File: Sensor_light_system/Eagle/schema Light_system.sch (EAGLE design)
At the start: 11 parts, among them IC1 STM32F030C8T6TR, J1 12_WAY_CON

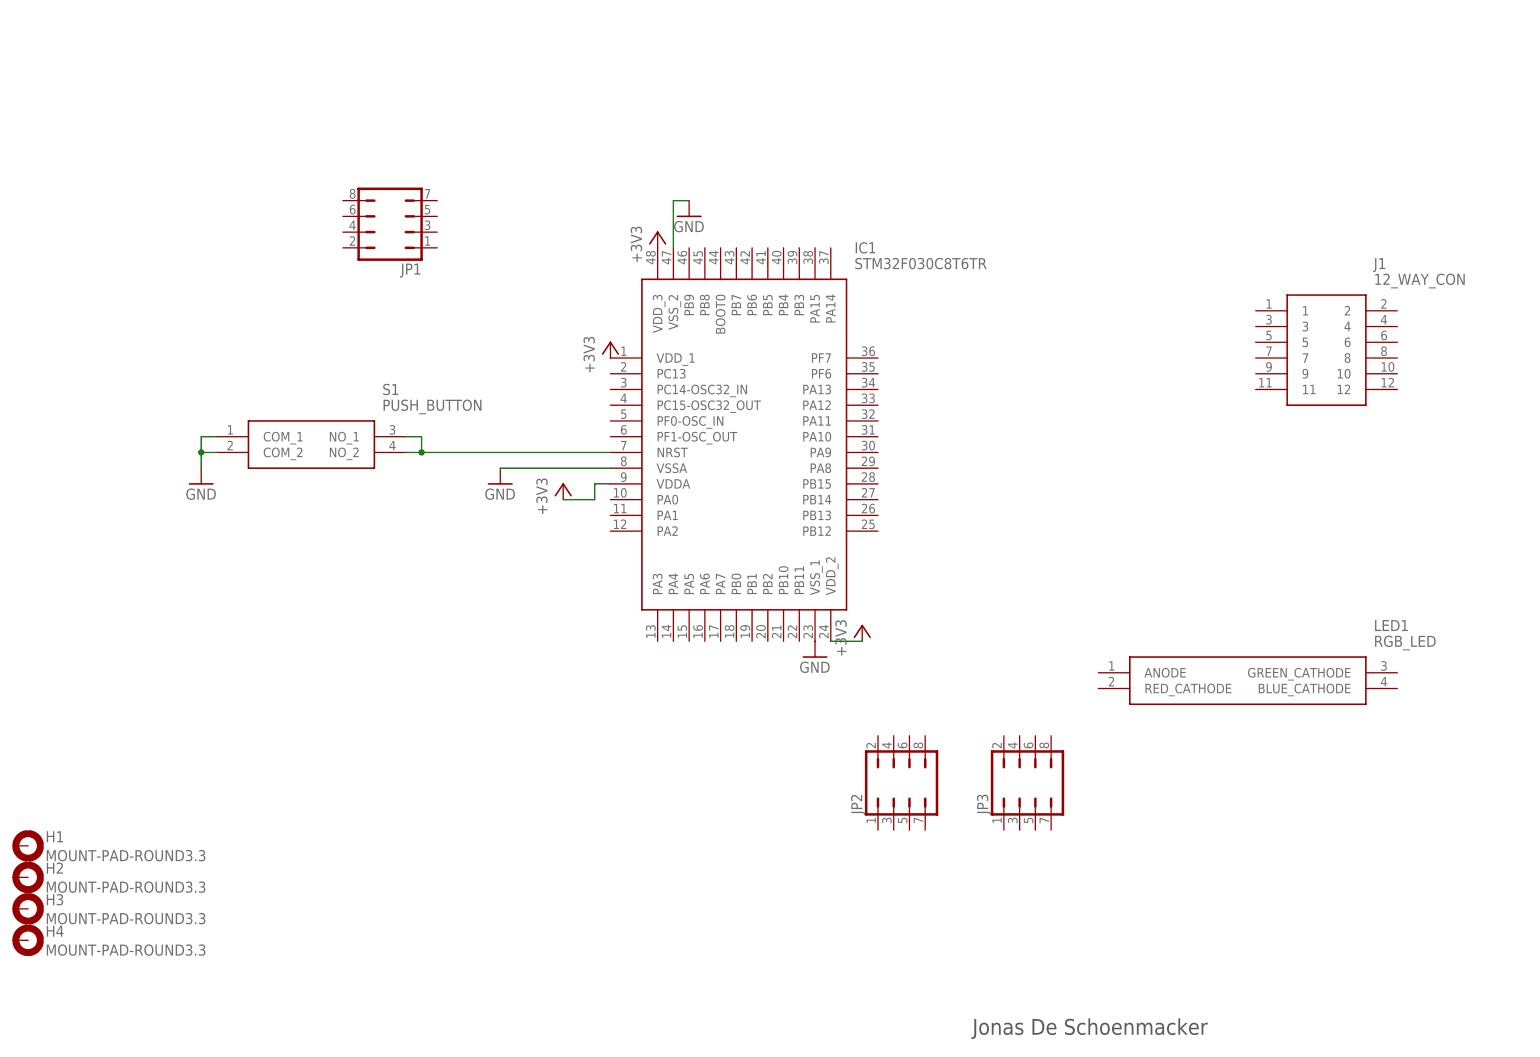
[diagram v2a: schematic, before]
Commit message: schema sensor
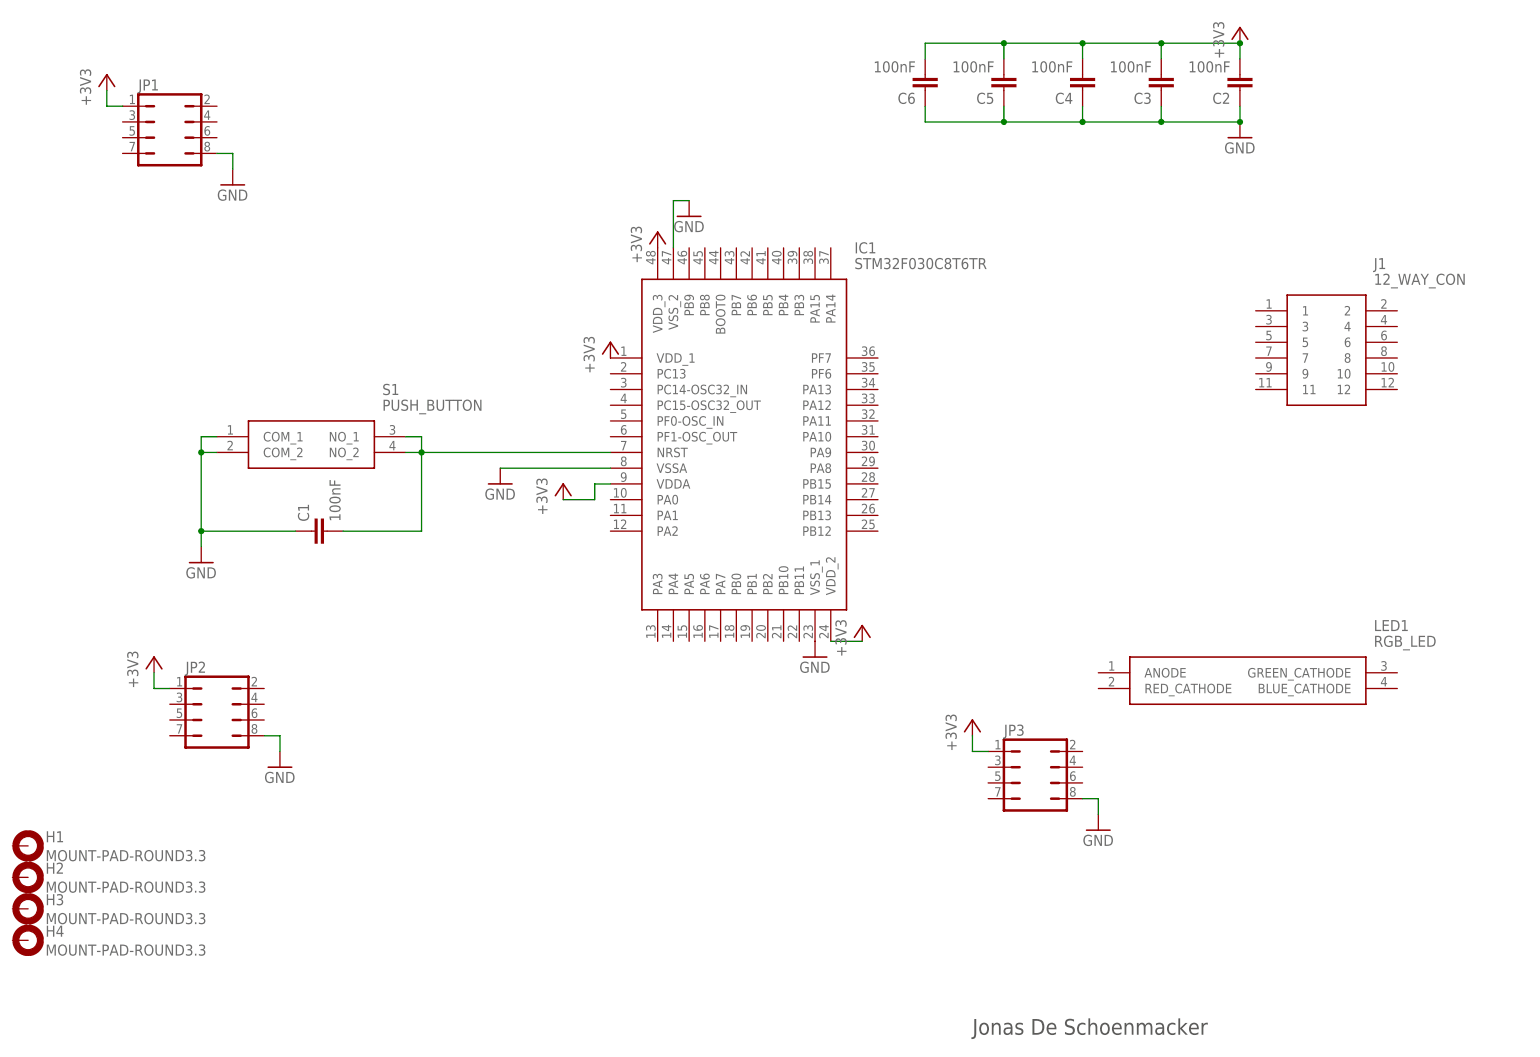
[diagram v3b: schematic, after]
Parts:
- added C1, C2, C3, C4, C5, C6: 100nF, resistor:C-EUC1206
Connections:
- new net OSC_IN: C2.2
- new net OSC_OUT: C1.2
- net +3V3: now also C2.2, C3.2, C4.1, C4.2, C5.1, C5.2, C6.1, C6.2
- net GND: now also C1.1, C2.1, C3.1, C3.2, C4.1, C4.2, C5.1, C5.2, C6.1, C6.2, JP1.8, JP2.8, JP3.8
- net N$3: now also C1.2
- net N$6: now also C3.1
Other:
- moved on the sheet: JP1, JP2, JP3
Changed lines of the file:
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@@
 <part name="JP2" library="jumper" deviceset="JP4Q" device=""/>
 <part name="JP3" library="jumper" deviceset="JP4Q" device=""/>
+<part name="+3V5" library="supply1" deviceset="+3V3" device=""/>
+<part name="GND5" library="supply1" deviceset="GND" device=""/>
+<part name="C1" library="resistor" deviceset="C-EU" device="C1206" value="100nF"/>
+<part name="+3V6" library="supply1" deviceset="+3V3" device=""/>
+<part name="C2" library="resistor" deviceset="C-EU" device="C1206" value="100nF"/>
+<part name="C3" library="resistor" deviceset="C-EU" device="C1206" value="100nF"/>
+<part name="C4" library="resistor" deviceset="C-EU" device="C1206" value="100nF"/>
+<part name="C5" library="resistor" deviceset="C-EU" device="C1206" value="100nF"/>
+<part name="C6" library="resistor" deviceset="C-EU" device="C1206" value="100nF"/>
+<part name="GND6" library="supply1" deviceset="GND" device=""/>
+<part name="+3V7" library="supply1" deviceset="+3V3" device=""/>
+<part name="GND7" library="supply1" deviceset="GND" device=""/>
+<part name="GND8" library="supply1" deviceset="GND" device=""/>
+<part name="+3V8" library="supply1" deviceset="+3V3" device=""/>
 </parts>
 <sheets>
@@
 <attribute name="VALUE" x="96.52" y="91.44" size="1.778" layer="96" rot="R90"/>
 </instance>
-<instance part="GND4" gate="1" x="40.64" y="96.52">
-<attribute name="VALUE" x="38.1" y="93.98" size="1.778" layer="96"/>
-</instance>
-<instance part="JP1" gate="B" x="71.12" y="137.16" rot="R90"/>
-<instance part="JP2" gate="B" x="152.4" y="48.26"/>
-<instance part="JP3" gate="B" x="172.72" y="48.26"/>
+<instance part="GND4" gate="1" x="40.64" y="83.82">
+<attribute name="VALUE" x="38.1" y="81.28" size="1.778" layer="96"/>
+</instance>
+<instance part="JP1" gate="B" x="35.56" y="154.94" rot="R270"/>
+<instance part="JP2" gate="B" x="43.18" y="60.96" rot="R270"/>
+<instance part="JP3" gate="B" x="175.26" y="50.8" rot="R270"/>
+<instance part="+3V5" gate="G$1" x="25.4" y="162.56">
+<attribute name="VALUE" x="22.86" y="157.48" size="1.778" layer="96" rot="R90"/>
+</instance>
+<instance part="GND5" gate="1" x="45.72" y="144.78">
+<attribute name="VALUE" x="43.18" y="142.24" size="1.778" layer="96"/>
+</instance>
+<instance part="C1" gate="G$1" x="58.42" y="88.9" rot="R90"/>
+<instance part="+3V6" gate="G$1" x="208.28" y="170.18">
+<attribute name="VALUE" x="205.74" y="165.1" size="1.778" layer="96" rot="R90"/>
+</instance>
+<instance part="C2" gate="G$1" x="208.28" y="160.02" rot="R180"/>
+<instance part="C3" gate="G$1" x="195.58" y="160.02" rot="R180"/>
+<instance part="C4" gate="G$1" x="182.88" y="160.02" rot="R180"/>
+<instance part="C5" gate="G$1" x="170.18" y="160.02" rot="R180"/>
+<instance part="C6" gate="G$1" x="157.48" y="160.02" rot="R180"/>
+<instance part="GND6" gate="1" x="208.28" y="152.4"/>
+<instance part="+3V7" gate="G$1" x="33.02" y="68.58">
+<attribute name="VALUE" x="30.48" y="63.5" size="1.778" layer="96" rot="R90"/>
+</instance>
+<instance part="GND7" gate="1" x="53.34" y="50.8">
+<attribute name="VALUE" x="50.8" y="48.26" size="1.778" layer="96"/>
+</instance>
+<instance part="GND8" gate="1" x="185.42" y="40.64">
+<attribute name="VALUE" x="182.88" y="38.1" size="1.778" layer="96"/>
+</instance>
+<instance part="+3V8" gate="G$1" x="165.1" y="58.42">
+<attribute name="VALUE" x="162.56" y="53.34" size="1.778" layer="96" rot="R90"/>
+</instance>
 </instances>
 <busses>
@@
 <pinref part="+3V2" gate="G$1" pin="+3V3"/>
 <wire x1="142.24" y1="71.12" x2="147.32" y2="71.12" width="0.1524" layer="91"/>
+</segment>
+<segment>
+<pinref part="+3V5" gate="G$1" pin="+3V3"/>
+<wire x1="25.4" y1="160.02" x2="25.4" y2="157.48" width="0.1524" layer="91"/>
+<pinref part="JP1" gate="B" pin="1"/>
+<wire x1="25.4" y1="157.48" x2="27.94" y2="157.48" width="0.1524" layer="91"/>
+</segment>
+<segment>
+<pinref part="+3V6" gate="G$1" pin="+3V3"/>
+<pinref part="C2" gate="G$1" pin="2"/>
+<wire x1="208.28" y1="167.64" x2="208.28" y2="165.1" width="0.1524" layer="91"/>
+<pinref part="C6" gate="G$1" pin="2"/>
+<wire x1="208.28" y1="167.64" x2="195.58" y2="167.64" width="0.1524" layer="91"/>
+<wire x1="195.58" y1="167.64" x2="182.88" y2="167.64" width="0.1524" layer="91"/>
+<wire x1="182.88" y1="167.64" x2="170.18" y2="167.64" width="0.1524" layer="91"/>
+<wire x1="170.18" y1="167.64" x2="157.48" y2="167.64" width="0.1524" layer="91"/>
+<wire x1="157.48" y1="167.64" x2="157.48" y2="165.1" width="0.1524" layer="91"/>
+<junction x="208.28" y="167.64"/>
+<pinref part="C5" gate="G$1" pin="2"/>
+<wire x1="170.18" y1="165.1" x2="170.18" y2="167.64" width="0.1524" layer="91"/>
+<junction x="170.18" y="167.64"/>
+<pinref part="C4" gate="G$1" pin="2"/>
+<wire x1="182.88" y1="165.1" x2="182.88" y2="167.64" width="0.1524" layer="91"/>
+<junction x="182.88" y="167.64"/>
+<pinref part="C3" gate="G$1" pin="2"/>
+<wire x1="195.58" y1="165.1" x2="195.58" y2="167.64" width="0.1524" layer="91"/>
+<junction x="195.58" y="167.64"/>
+</segment>
+<segment>
+<pinref part="+3V7" gate="G$1" pin="+3V3"/>
+<wire x1="33.02" y1="66.04" x2="33.02" y2="63.5" width="0.1524" layer="91"/>
+<pinref part="JP2" gate="B" pin="1"/>
+<wire x1="33.02" y1="63.5" x2="35.56" y2="63.5" width="0.1524" layer="91"/>
+</segment>
+<segment>
+<pinref part="JP3" gate="B" pin="1"/>
+<wire x1="167.64" y1="53.34" x2="165.1" y2="53.34" width="0.1524" layer="91"/>
+<pinref part="+3V8" gate="G$1" pin="+3V3"/>
+<wire x1="165.1" y1="53.34" x2="165.1" y2="55.88" width="0.1524" layer="91"/>
 </segment>
 </net>
@@
 <wire x1="40.64" y1="101.6" x2="43.18" y2="101.6" width="0.1524" layer="91"/>
 <pinref part="GND4" gate="1" pin="GND"/>
-<wire x1="40.64" y1="99.06" x2="40.64" y2="101.6" width="0.1524" layer="91"/>
+<wire x1="40.64" y1="86.36" x2="40.64" y2="88.9" width="0.1524" layer="91"/>
 <junction x="40.64" y="101.6"/>
+<pinref part="C1" gate="G$1" pin="1"/>
+<wire x1="40.64" y1="88.9" x2="40.64" y2="101.6" width="0.1524" layer="91"/>
+<wire x1="55.88" y1="88.9" x2="40.64" y2="88.9" width="0.1524" layer="91"/>
+<junction x="40.64" y="88.9"/>
+</segment>
+<segment>
+<pinref part="JP1" gate="B" pin="8"/>
+<wire x1="43.18" y1="149.86" x2="45.72" y2="149.86" width="0.1524" layer="91"/>
+<pinref part="GND5" gate="1" pin="GND"/>
+<wire x1="45.72" y1="149.86" x2="45.72" y2="147.32" width="0.1524" layer="91"/>
+</segment>
+<segment>
+<pinref part="C6" gate="G$1" pin="1"/>
+<wire x1="157.48" y1="157.48" x2="157.48" y2="154.94" width="0.1524" layer="91"/>
+<pinref part="C2" gate="G$1" pin="1"/>
+<wire x1="157.48" y1="154.94" x2="170.18" y2="154.94" width="0.1524" layer="91"/>
+<wire x1="170.18" y1="154.94" x2="182.88" y2="154.94" width="0.1524" layer="91"/>
+<wire x1="182.88" y1="154.94" x2="195.58" y2="154.94" width="0.1524" layer="91"/>
+<wire x1="195.58" y1="154.94" x2="208.28" y2="154.94" width="0.1524" layer="91"/>
+<wire x1="208.28" y1="154.94" x2="208.28" y2="157.48" width="0.1524" layer="91"/>
+<pinref part="C3" gate="G$1" pin="1"/>
+<wire x1="195.58" y1="157.48" x2="195.58" y2="154.94" width="0.1524" layer="91"/>
+<junction x="195.58" y="154.94"/>
+<pinref part="C4" gate="G$1" pin="1"/>
+<wire x1="182.88" y1="157.48" x2="182.88" y2="154.94" width="0.1524" layer="91"/>
+<junction x="182.88" y="154.94"/>
+<pinref part="C5" gate="G$1" pin="1"/>
+<wire x1="170.18" y1="157.48" x2="170.18" y2="154.94" width="0.1524" layer="91"/>
+<junction x="170.18" y="154.94"/>
+<pinref part="GND6" gate="1" pin="GND"/>
+<junction x="208.28" y="154.94"/>
+</segment>
+<segment>
+<pinref part="JP2" gate="B" pin="8"/>
+<wire x1="50.8" y1="55.88" x2="53.34" y2="55.88" width="0.1524" layer="91"/>
+<pinref part="GND7" gate="1" pin="GND"/>
+<wire x1="53.34" y1="55.88" x2="53.34" y2="53.34" width="0.1524" layer="91"/>
+</segment>
+<segment>
+<pinref part="JP3" gate="B" pin="8"/>
+<wire x1="182.88" y1="45.72" x2="185.42" y2="45.72" width="0.1524" layer="91"/>
+<pinref part="GND8" gate="1" pin="GND"/>
+<wire x1="185.42" y1="45.72" x2="185.42" y2="43.18" width="0.1524" layer="91"/>
 </segment>
 </net>
@@
 <wire x1="106.68" y1="101.6" x2="76.2" y2="101.6" width="0.1524" layer="91"/>
 <junction x="76.2" y="101.6"/>
+<pinref part="C1" gate="G$1" pin="2"/>
+<wire x1="63.5" y1="88.9" x2="76.2" y2="88.9" width="0.1524" layer="91"/>
+<wire x1="76.2" y1="88.9" x2="76.2" y2="101.6" width="0.1524" layer="91"/>
 </segment>
 </net>

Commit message: schema sensor gewijzigd
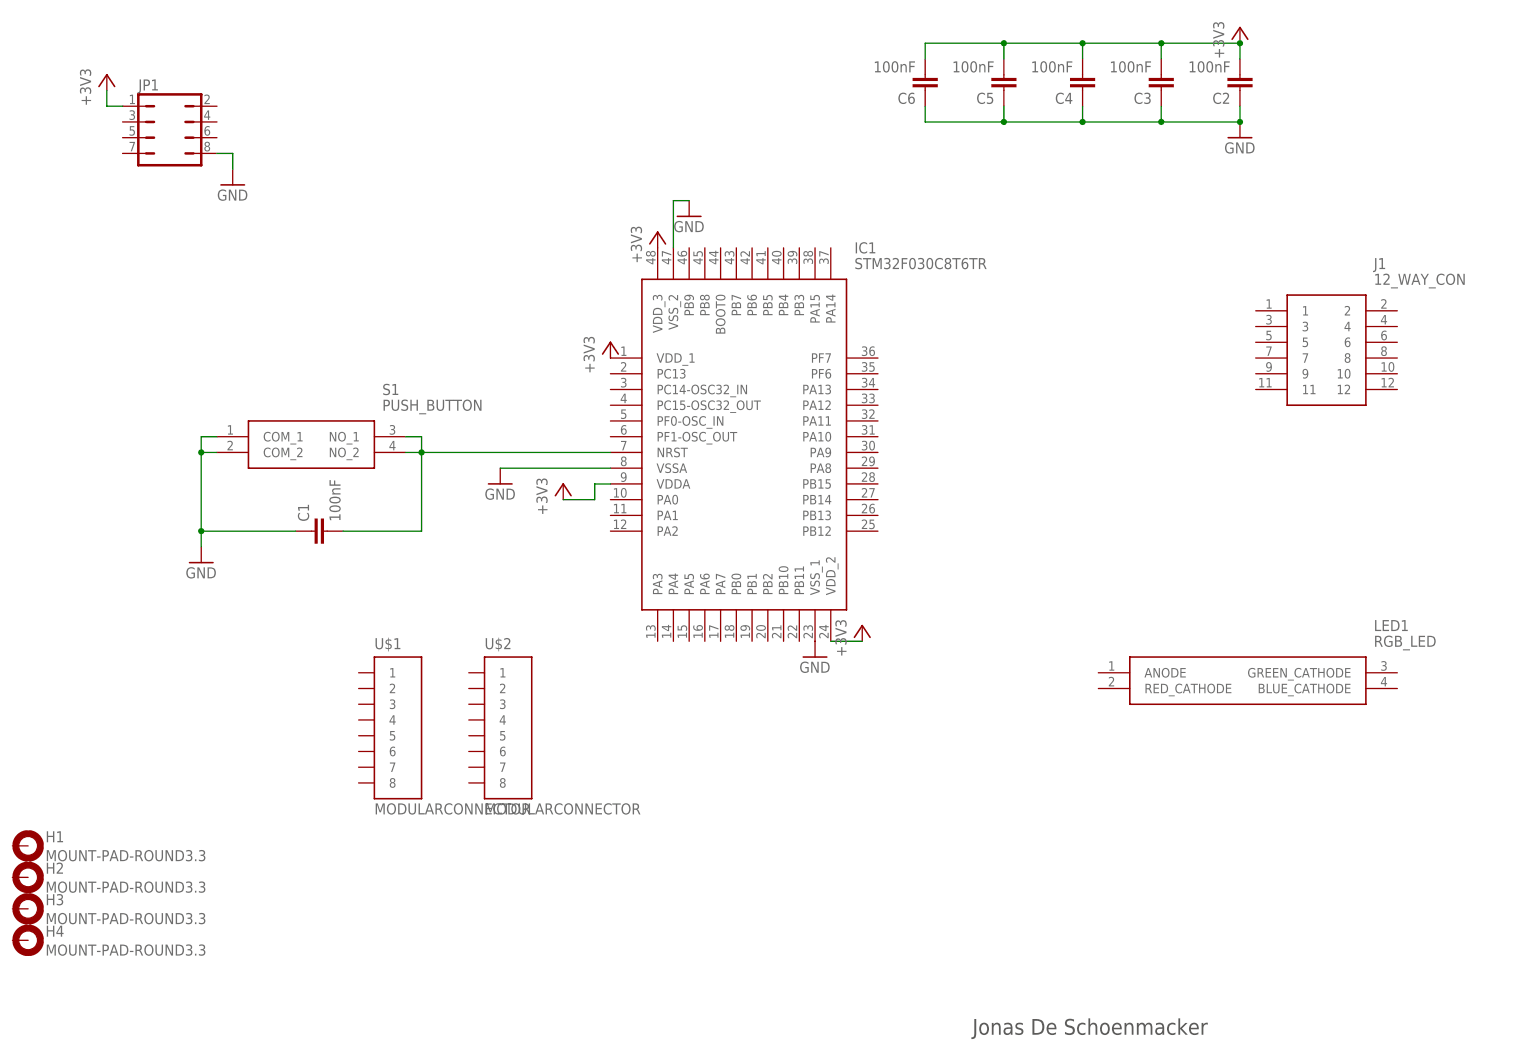
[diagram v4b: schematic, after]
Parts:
- removed JP2, JP3: (no value), jumper:JP4Q
- added U$1, U$2: MODULARCONNECTOR, Main_lib:MODULARCONNECTOR
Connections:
- removed net N$5: JP2.2
- net +3V3: no longer JP2.1, JP3.1
- net GND: no longer JP2.3, JP2.8, JP3.3, JP3.8
- net N$3: no longer JP3.2
